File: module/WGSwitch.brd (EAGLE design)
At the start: 32.7 x 55.5 mm, 26 parts, among them Q1 MMBT3904, Q2 MMBT3904, Q3 MMBT3904, U1 7805TV, U2 ARDUINO_PRO_MINI

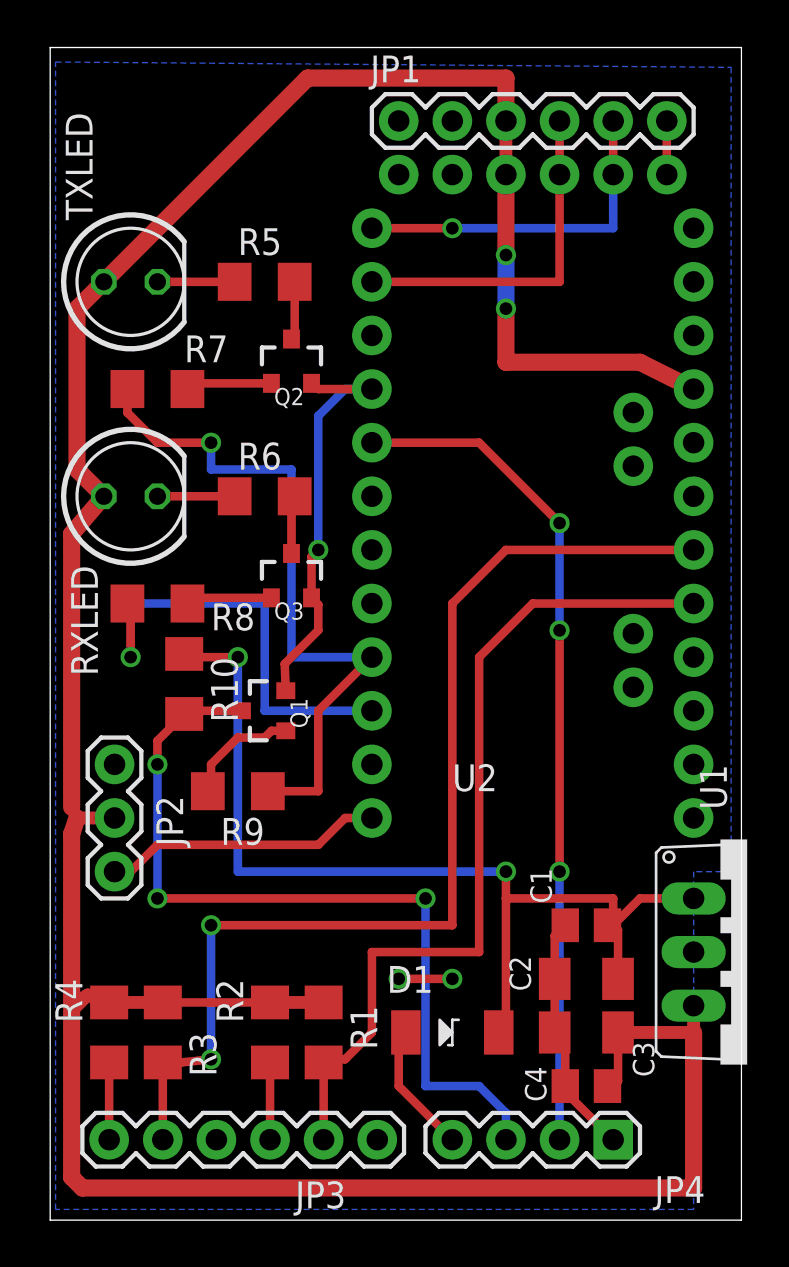
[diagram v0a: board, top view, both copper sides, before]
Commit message: cleanup and optimize TRSwitchSleep to eliminate extra delay.
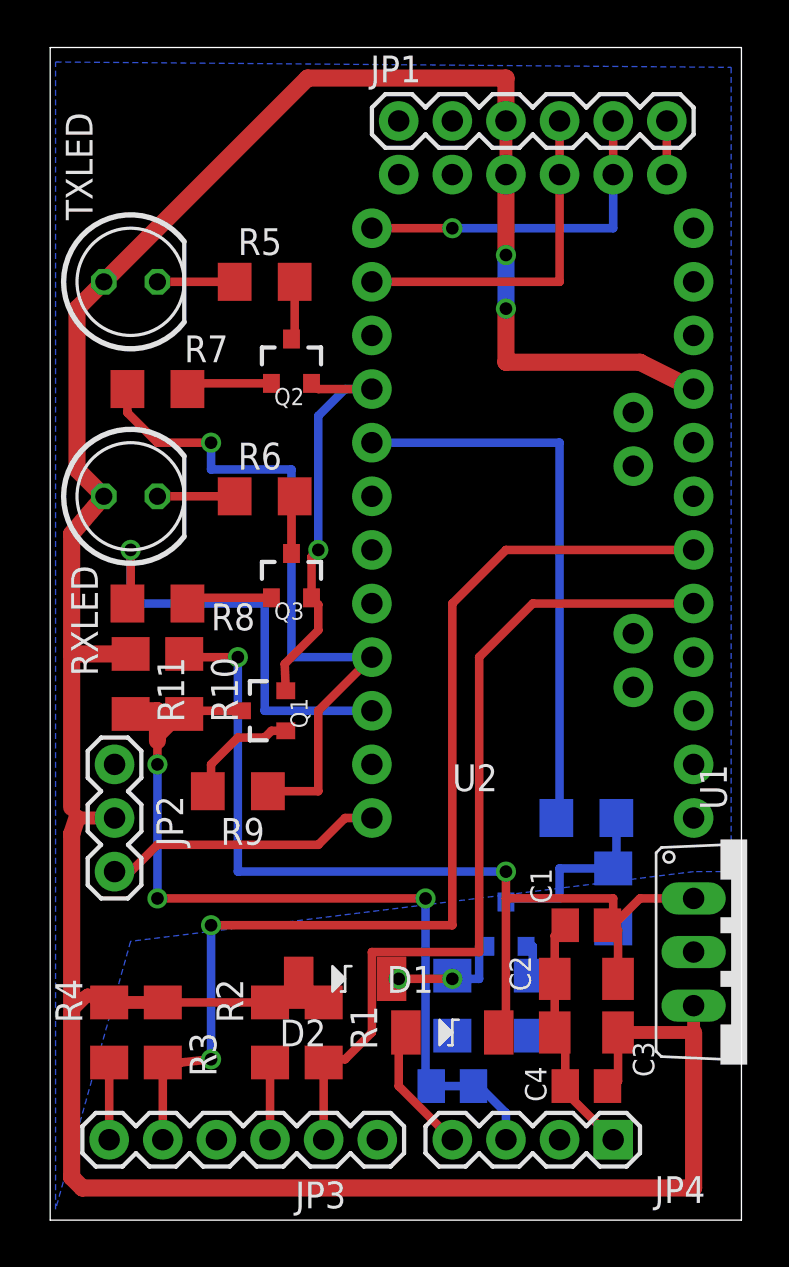
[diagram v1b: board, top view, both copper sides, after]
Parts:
- added C5: 0.1, rcl:C0805K
- added D2: PMEG3030EP, kb1vc_robot_parts:SOD128
- added Q4: PMBT3906, SparkFun-DiscreteSemi:SOT23-3
- added R11, R12, R13, R14, R15: 10K, rcl:R1206
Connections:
- removed net PTT_IN_L: JP4.2, U2.5
- new net N$12: Q4.3, R14.2, R15.2
- new net N$5: D2.P$2, Q4.2, R12.2
- new net N$9: Q4.1, R13.1
- new net PTT_H: R15.1, U2.5
- new net PTT_IN_RAW_L: C5.1, JP4.2, R12.1, R13.2
- net GND: now also C5.2, R14.1
- net TX_EN_OUT_L: now also R11.2
- net VCC: now also D2.P$1, R11.1
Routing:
- net PTT_IN_L: track 39.7 -> 0.00 mm, vias 3 -> 0
- net PTT_H: track 0.00 -> 26.8 mm
- net N$12: track 0.00 -> 9.21 mm
- net N$5: track 0.00 -> 3.28 mm
- net TX_EN_OUT_L: track 39.2 -> 42.1 mm
- net VCC: track 149.5 -> 152.3 mm
- net N$9: track 0.00 -> 1.71 mm
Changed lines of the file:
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@@
 <?xml version="1.0" encoding="utf-8"?>
 <!DOCTYPE eagle SYSTEM "eagle.dtd">
-<eagle version="7.5.0">
+<eagle version="7.3.0">
 <drawing>
 <settings>
@@
 <layer number="19" name="Unrouted" color="6" fill="1" visible="yes" active="yes"/>
 <layer number="20" name="Dimension" color="15" fill="1" visible="yes" active="yes"/>
-<layer number="21" name="tPlace" color="7" fill="1" visible="yes" active="yes"/>
-<layer number="22" name="bPlace" color="7" fill="1" visible="yes" active="yes"/>
+<layer number="21" name="tPlace" color="7" fill="1" visible="no" active="yes"/>
+<layer number="22" name="bPlace" color="7" fill="1" visible="no" active="yes"/>
 <layer number="23" name="tOrigins" color="15" fill="1" visible="yes" active="yes"/>
 <layer number="24" name="bOrigins" color="15" fill="1" visible="yes" active="yes"/>
@@
 <attribute name="VALUE" x="25.4" y="17.78" size="1.27" layer="27" ratio="10" rot="R270"/>
 </element>
+<element name="R11" library="rcl" package="R1206" value="10K" x="3.81" y="25.4" rot="R270"/>
+<element name="Q4" library="SparkFun-DiscreteSemi" package="SOT23-3" value="PMBT3906" x="21.59" y="13.97" rot="MR0">
+<attribute name="PROD_ID" value="TRANS-08052" x="21.59" y="13.97" size="1.778" layer="28" rot="MR0" display="off"/>
+</element>
+<element name="D2" library="kb1vc_robot_parts" package="SOD128" value="PMEG3030EP" x="13.97" y="11.43"/>
+<element name="R12" library="rcl" package="R1206" value="10K" x="19.05" y="10.16" rot="MR90"/>
+<element name="R13" library="rcl" package="R1206" value="10K" x="22.86" y="10.16" rot="MR270"/>
+<element name="C5" library="rcl" package="C0805K" value="0.1" x="19.05" y="6.35" rot="MR0"/>
+<element name="R14" library="rcl" package="R1206" value="10K" x="26.67" y="15.24" rot="MR90"/>
+<element name="R15" library="rcl" package="R1206" value="10K" x="25.4" y="19.05" rot="MR180"/>
 </elements>
 <signals>
@@
 <vertex x="32.258" y="16.51"/>
 <vertex x="30.48" y="16.51"/>
-<vertex x="30.48" y="0.508"/>
+<vertex x="3.81" y="13.208"/>
 <vertex x="0.254" y="0.508"/>
 </polygon>
@@
 <via x="19.05" y="11.43" extent="1-16" drill="0.6" shape="square"/>
 <wire x1="16.51" y1="11.43" x2="19.05" y2="11.43" width="0.4064" layer="1"/>
+<contactref element="C5" pad="2"/>
+<contactref element="R14" pad="1"/>
+<wire x1="26.67" y1="13.818" x2="30.48" y2="12.7" width="0" layer="19" extent="16-16"/>
+<wire x1="24.4" y1="13.97" x2="26.67" y2="13.818" width="0" layer="19" extent="1-16"/>
+<wire x1="19.05" y1="11.43" x2="23.9" y2="11.43" width="0" layer="19" extent="1-1"/>
+<wire x1="18.05" y1="6.35" x2="19.05" y2="11.43" width="0" layer="19" extent="16-16"/>
+<wire x1="15.494" y1="3.81" x2="18.05" y2="6.35" width="0" layer="19" extent="16-16"/>
+<wire x1="7.874" y1="3.81" x2="15.494" y2="3.81" width="0" layer="19" extent="1-1"/>
+<wire x1="11.16" y1="25.08" x2="16.51" y2="11.43" width="0" layer="19" extent="1-1"/>
 </signal>
 <signal name="VCC">
@@
 <wire x1="3.048" y1="19.05" x2="1.27" y2="19.05" width="0.6096" layer="1"/>
 <wire x1="1.27" y1="19.05" x2="1.016" y2="19.558" width="0.6096" layer="1"/>
-<wire x1="1.016" y1="19.558" x2="1.016" y2="32.512" width="0.8128" layer="1"/>
+<wire x1="1.016" y1="19.558" x2="1.016" y2="26.822" width="0.8128" layer="1"/>
+<wire x1="1.016" y1="26.822" x2="1.016" y2="32.512" width="0.8128" layer="1"/>
 <wire x1="1.016" y1="32.512" x2="2.54" y2="34.29" width="0.8128" layer="1"/>
 <wire x1="2.54" y1="44.45" x2="12.192" y2="54.102" width="0.8128" layer="1"/>
@@
 <wire x1="1.016" y1="9.906" x2="1.778" y2="10.668" width="0.6096" layer="1"/>
 <wire x1="5.334" y1="10.312" x2="10.414" y2="10.312" width="0.4064" layer="1"/>
+<contactref element="R11" pad="1"/>
+<wire x1="3.81" y1="26.822" x2="1.016" y2="26.822" width="0.8128" layer="1"/>
+<contactref element="D2" pad="P$1"/>
+<wire x1="12.954" y1="10.312" x2="11.77" y2="11.43" width="0" layer="19" extent="1-1"/>
 </signal>
 <signal name="N$10">
@@
 <contactref element="R8" pad="1"/>
 <contactref element="U2" pad="10"/>
-<via x="3.81" y="26.67" extent="1-16" drill="0.6" shape="square"/>
-<wire x1="3.81" y1="26.67" x2="3.81" y2="29.058" width="0.4064" layer="1"/>
+<via x="3.81" y="31.75" extent="1-16" drill="0.6" shape="square"/>
+<wire x1="3.81" y1="31.75" x2="3.81" y2="29.058" width="0.4064" layer="1"/>
 <wire x1="3.81" y1="29.058" x2="3.658" y2="29.21" width="0.4064" layer="1"/>
-<wire x1="3.81" y1="26.67" x2="3.81" y2="29.21" width="0.4064" layer="16"/>
+<wire x1="3.81" y1="31.75" x2="3.81" y2="29.21" width="0.4064" layer="16"/>
 <wire x1="3.81" y1="29.21" x2="10.16" y2="29.21" width="0.4064" layer="16"/>
 <wire x1="10.16" y1="29.21" x2="10.16" y2="24.13" width="0.4064" layer="16"/>
@@
 <wire x1="7.62" y1="36.83" x2="5.08" y2="36.83" width="0.4064" layer="1"/>
 <wire x1="5.08" y1="36.83" x2="3.658" y2="38.252" width="0.4064" layer="1"/>
-</signal>
-<signal name="PTT_IN_L">
-<contactref element="JP4" pad="2"/>
-<contactref element="U2" pad="5"/>
-<wire x1="15.24" y1="36.83" x2="20.32" y2="36.83" width="0.4064" layer="1"/>
-<wire x1="20.32" y1="36.83" x2="24.13" y2="33.02" width="0.4064" layer="1"/>
-<via x="24.13" y="33.02" extent="1-16" drill="0.6" shape="square"/>
-<wire x1="24.13" y1="33.02" x2="24.13" y2="27.94" width="0.4064" layer="16"/>
-<via x="24.13" y="27.94" extent="1-16" drill="0.6" shape="square"/>
-<wire x1="24.13" y1="27.94" x2="24.13" y2="16.51" width="0.4064" layer="1"/>
-<via x="24.13" y="16.51" extent="1-16" drill="0.6" shape="square"/>
-<wire x1="24.13" y1="16.51" x2="24.13" y2="3.81" width="0.4064" layer="16"/>
 </signal>
 <signal name="TX_EN_OUT_L">
@@
 <wire x1="20.32" y1="6.35" x2="21.59" y2="5.08" width="0.4064" layer="16"/>
 <wire x1="21.59" y1="5.08" x2="21.59" y2="3.81" width="0.4064" layer="16"/>
+<contactref element="R11" pad="2"/>
+<wire x1="5.08" y1="22.708" x2="5.08" y2="24.13" width="0.8128" layer="1"/>
+<wire x1="5.08" y1="24.13" x2="3.81" y2="24.13" width="0.8128" layer="1"/>
+<wire x1="3.81" y1="24.13" x2="3.81" y2="23.978" width="0.8128" layer="1"/>
 </signal>
 <signal name="N$2">
@@
 <wire x1="6.772" y1="39.64" x2="6.502" y2="39.37" width="0.4064" layer="1"/>
 </signal>
+<signal name="PTT_IN_RAW_L">
+<contactref element="JP4" pad="2"/>
+<contactref element="R12" pad="1"/>
+<contactref element="C5" pad="1"/>
+<contactref element="R13" pad="2"/>
+<wire x1="20.05" y1="6.35" x2="22.86" y2="8.738" width="0" layer="19" extent="16-16"/>
+<wire x1="19.05" y1="8.738" x2="20.05" y2="6.35" width="0" layer="19" extent="16-16"/>
+<wire x1="24.13" y1="3.81" x2="20.05" y2="6.35" width="0" layer="19" extent="16-16"/>
+</signal>
+<signal name="N$5">
+<contactref element="D2" pad="P$2"/>
+<contactref element="Q4" pad="2"/>
+<contactref element="R12" pad="2"/>
+<wire x1="16.17" y1="11.43" x2="19.05" y2="11.582" width="0" layer="19" extent="1-16"/>
+<wire x1="20.64" y1="12.97" x2="20.32" y2="12.97" width="0.4064" layer="16"/>
+<wire x1="20.32" y1="12.97" x2="20.32" y2="11.43" width="0.4064" layer="16"/>
+<wire x1="20.32" y1="11.43" x2="19.05" y2="11.43" width="0.4064" layer="16"/>
+<wire x1="19.05" y1="11.43" x2="19.05" y2="11.582" width="0.4064" layer="16"/>
+</signal>
+<signal name="N$9">
+<contactref element="Q4" pad="1"/>
+<contactref element="R13" pad="1"/>
+<wire x1="22.54" y1="12.97" x2="22.86" y2="12.97" width="0.4064" layer="16"/>
+<wire x1="22.86" y1="12.97" x2="22.86" y2="11.582" width="0.4064" layer="16"/>
+</signal>
+<signal name="N$12">
+<contactref element="Q4" pad="3"/>
+<contactref element="R14" pad="2"/>
+<contactref element="R15" pad="2"/>
+<wire x1="26.67" y1="16.662" x2="26.822" y2="16.662" width="0.4064" layer="16"/>
+<wire x1="26.822" y1="16.662" x2="26.822" y2="19.05" width="0.4064" layer="16"/>
+<wire x1="26.67" y1="16.662" x2="24.13" y2="16.662" width="0.4064" layer="16"/>
+<wire x1="24.13" y1="16.662" x2="24.13" y2="15.24" width="0.4064" layer="16"/>
+<wire x1="24.13" y1="15.24" x2="21.59" y2="15.24" width="0.4064" layer="16"/>
+<wire x1="21.59" y1="15.24" x2="21.59" y2="15.07" width="0.4064" layer="16"/>
+</signal>
+<signal name="PTT_H">
+<contactref element="R15" pad="1"/>
+<contactref element="U2" pad="5"/>
+<wire x1="23.978" y1="19.05" x2="24.13" y2="19.05" width="0.4064" layer="16"/>
+<wire x1="24.13" y1="19.05" x2="24.13" y2="36.83" width="0.4064" layer="16"/>
+<wire x1="24.13" y1="36.83" x2="15.24" y2="36.83" width="0.4064" layer="16"/>
+</signal>
 </signals>

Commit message: Just about right.
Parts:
- removed C5: 0.1, rcl:C0805K
- removed D2: PMEG3030EP, kb1vc_robot_parts:SOD128
- removed Q4: PMBT3906, SparkFun-DiscreteSemi:SOT23-3
- removed R11, R12, R13, R14, R15: 10K, rcl:R1206
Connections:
- removed net N$12: Q4.3, R14.2, R15.2
- removed net N$5: D2.P$2, Q4.2, R12.2
- removed net N$9: Q4.1, R13.1
- removed net PTT_H: R15.1, U2.5
- removed net PTT_IN_RAW_L: C5.1, JP4.2, R12.1, R13.2
- new net PTT_IN_L: JP4.2, U2.5
- net GND: no longer C5.2, R14.1
- net TX_EN_OUT_L: no longer R11.2
- net VCC: no longer D2.P$1, R11.1
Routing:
- net PTT_IN_L: track 0.00 -> 39.7 mm, vias 0 -> 3
- net PTT_H: track 26.8 -> 0.00 mm
- net N$12: track 9.21 -> 0.00 mm
- net N$5: track 3.28 -> 0.00 mm
- net TX_EN_OUT_L: track 42.1 -> 39.2 mm
- net VCC: track 152.3 -> 149.5 mm
- net N$9: track 1.71 -> 0.00 mm
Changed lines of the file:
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@@
 <?xml version="1.0" encoding="utf-8"?>
 <!DOCTYPE eagle SYSTEM "eagle.dtd">
-<eagle version="7.3.0">
+<eagle version="7.5.0">
 <drawing>
 <settings>
@@
 <layer number="19" name="Unrouted" color="6" fill="1" visible="yes" active="yes"/>
 <layer number="20" name="Dimension" color="15" fill="1" visible="yes" active="yes"/>
-<layer number="21" name="tPlace" color="7" fill="1" visible="no" active="yes"/>
-<layer number="22" name="bPlace" color="7" fill="1" visible="no" active="yes"/>
+<layer number="21" name="tPlace" color="7" fill="1" visible="yes" active="yes"/>
+<layer number="22" name="bPlace" color="7" fill="1" visible="yes" active="yes"/>
 <layer number="23" name="tOrigins" color="15" fill="1" visible="yes" active="yes"/>
 <layer number="24" name="bOrigins" color="15" fill="1" visible="yes" active="yes"/>
@@
 <attribute name="VALUE" x="25.4" y="17.78" size="1.27" layer="27" ratio="10" rot="R270"/>
 </element>
-<element name="R11" library="rcl" package="R1206" value="10K" x="3.81" y="25.4" rot="R270"/>
-<element name="Q4" library="SparkFun-DiscreteSemi" package="SOT23-3" value="PMBT3906" x="21.59" y="13.97" rot="MR0">
-<attribute name="PROD_ID" value="TRANS-08052" x="21.59" y="13.97" size="1.778" layer="28" rot="MR0" display="off"/>
-</element>
-<element name="D2" library="kb1vc_robot_parts" package="SOD128" value="PMEG3030EP" x="13.97" y="11.43"/>
-<element name="R12" library="rcl" package="R1206" value="10K" x="19.05" y="10.16" rot="MR90"/>
-<element name="R13" library="rcl" package="R1206" value="10K" x="22.86" y="10.16" rot="MR270"/>
-<element name="C5" library="rcl" package="C0805K" value="0.1" x="19.05" y="6.35" rot="MR0"/>
-<element name="R14" library="rcl" package="R1206" value="10K" x="26.67" y="15.24" rot="MR90"/>
-<element name="R15" library="rcl" package="R1206" value="10K" x="25.4" y="19.05" rot="MR180"/>
 </elements>
 <signals>
@@
 <vertex x="32.258" y="16.51"/>
 <vertex x="30.48" y="16.51"/>
-<vertex x="3.81" y="13.208"/>
+<vertex x="30.48" y="0.508"/>
 <vertex x="0.254" y="0.508"/>
 </polygon>
@@
 <via x="19.05" y="11.43" extent="1-16" drill="0.6" shape="square"/>
 <wire x1="16.51" y1="11.43" x2="19.05" y2="11.43" width="0.4064" layer="1"/>
-<contactref element="C5" pad="2"/>
-<contactref element="R14" pad="1"/>
-<wire x1="26.67" y1="13.818" x2="30.48" y2="12.7" width="0" layer="19" extent="16-16"/>
-<wire x1="24.4" y1="13.97" x2="26.67" y2="13.818" width="0" layer="19" extent="1-16"/>
-<wire x1="19.05" y1="11.43" x2="23.9" y2="11.43" width="0" layer="19" extent="1-1"/>
-<wire x1="18.05" y1="6.35" x2="19.05" y2="11.43" width="0" layer="19" extent="16-16"/>
-<wire x1="15.494" y1="3.81" x2="18.05" y2="6.35" width="0" layer="19" extent="16-16"/>
-<wire x1="7.874" y1="3.81" x2="15.494" y2="3.81" width="0" layer="19" extent="1-1"/>
-<wire x1="11.16" y1="25.08" x2="16.51" y2="11.43" width="0" layer="19" extent="1-1"/>
 </signal>
 <signal name="VCC">
@@
 <wire x1="3.048" y1="19.05" x2="1.27" y2="19.05" width="0.6096" layer="1"/>
 <wire x1="1.27" y1="19.05" x2="1.016" y2="19.558" width="0.6096" layer="1"/>
-<wire x1="1.016" y1="19.558" x2="1.016" y2="26.822" width="0.8128" layer="1"/>
-<wire x1="1.016" y1="26.822" x2="1.016" y2="32.512" width="0.8128" layer="1"/>
+<wire x1="1.016" y1="19.558" x2="1.016" y2="32.512" width="0.8128" layer="1"/>
 <wire x1="1.016" y1="32.512" x2="2.54" y2="34.29" width="0.8128" layer="1"/>
 <wire x1="2.54" y1="44.45" x2="12.192" y2="54.102" width="0.8128" layer="1"/>
@@
 <wire x1="1.016" y1="9.906" x2="1.778" y2="10.668" width="0.6096" layer="1"/>
 <wire x1="5.334" y1="10.312" x2="10.414" y2="10.312" width="0.4064" layer="1"/>
-<contactref element="R11" pad="1"/>
-<wire x1="3.81" y1="26.822" x2="1.016" y2="26.822" width="0.8128" layer="1"/>
-<contactref element="D2" pad="P$1"/>
-<wire x1="12.954" y1="10.312" x2="11.77" y2="11.43" width="0" layer="19" extent="1-1"/>
 </signal>
 <signal name="N$10">
@@
 <contactref element="R8" pad="1"/>
 <contactref element="U2" pad="10"/>
-<via x="3.81" y="31.75" extent="1-16" drill="0.6" shape="square"/>
-<wire x1="3.81" y1="31.75" x2="3.81" y2="29.058" width="0.4064" layer="1"/>
+<via x="3.81" y="26.67" extent="1-16" drill="0.6" shape="square"/>
+<wire x1="3.81" y1="26.67" x2="3.81" y2="29.058" width="0.4064" layer="1"/>
 <wire x1="3.81" y1="29.058" x2="3.658" y2="29.21" width="0.4064" layer="1"/>
-<wire x1="3.81" y1="31.75" x2="3.81" y2="29.21" width="0.4064" layer="16"/>
+<wire x1="3.81" y1="26.67" x2="3.81" y2="29.21" width="0.4064" layer="16"/>
 <wire x1="3.81" y1="29.21" x2="10.16" y2="29.21" width="0.4064" layer="16"/>
 <wire x1="10.16" y1="29.21" x2="10.16" y2="24.13" width="0.4064" layer="16"/>
@@
 <wire x1="7.62" y1="36.83" x2="5.08" y2="36.83" width="0.4064" layer="1"/>
 <wire x1="5.08" y1="36.83" x2="3.658" y2="38.252" width="0.4064" layer="1"/>
+</signal>
+<signal name="PTT_IN_L">
+<contactref element="JP4" pad="2"/>
+<contactref element="U2" pad="5"/>
+<wire x1="15.24" y1="36.83" x2="20.32" y2="36.83" width="0.4064" layer="1"/>
+<wire x1="20.32" y1="36.83" x2="24.13" y2="33.02" width="0.4064" layer="1"/>
+<via x="24.13" y="33.02" extent="1-16" drill="0.6" shape="square"/>
+<wire x1="24.13" y1="33.02" x2="24.13" y2="27.94" width="0.4064" layer="16"/>
+<via x="24.13" y="27.94" extent="1-16" drill="0.6" shape="square"/>
+<wire x1="24.13" y1="27.94" x2="24.13" y2="16.51" width="0.4064" layer="1"/>
+<via x="24.13" y="16.51" extent="1-16" drill="0.6" shape="square"/>
+<wire x1="24.13" y1="16.51" x2="24.13" y2="3.81" width="0.4064" layer="16"/>
 </signal>
 <signal name="TX_EN_OUT_L">
@@
 <wire x1="20.32" y1="6.35" x2="21.59" y2="5.08" width="0.4064" layer="16"/>
 <wire x1="21.59" y1="5.08" x2="21.59" y2="3.81" width="0.4064" layer="16"/>
-<contactref element="R11" pad="2"/>
-<wire x1="5.08" y1="22.708" x2="5.08" y2="24.13" width="0.8128" layer="1"/>
-<wire x1="5.08" y1="24.13" x2="3.81" y2="24.13" width="0.8128" layer="1"/>
-<wire x1="3.81" y1="24.13" x2="3.81" y2="23.978" width="0.8128" layer="1"/>
 </signal>
 <signal name="N$2">
@@
 <wire x1="6.772" y1="39.64" x2="6.502" y2="39.37" width="0.4064" layer="1"/>
 </signal>
-<signal name="PTT_IN_RAW_L">
-<contactref element="JP4" pad="2"/>
-<contactref element="R12" pad="1"/>
-<contactref element="C5" pad="1"/>
-<contactref element="R13" pad="2"/>
-<wire x1="20.05" y1="6.35" x2="22.86" y2="8.738" width="0" layer="19" extent="16-16"/>
-<wire x1="19.05" y1="8.738" x2="20.05" y2="6.35" width="0" layer="19" extent="16-16"/>
-<wire x1="24.13" y1="3.81" x2="20.05" y2="6.35" width="0" layer="19" extent="16-16"/>
-</signal>
-<signal name="N$5">
-<contactref element="D2" pad="P$2"/>
-<contactref element="Q4" pad="2"/>
-<contactref element="R12" pad="2"/>
-<wire x1="16.17" y1="11.43" x2="19.05" y2="11.582" width="0" layer="19" extent="1-16"/>
-<wire x1="20.64" y1="12.97" x2="20.32" y2="12.97" width="0.4064" layer="16"/>
-<wire x1="20.32" y1="12.97" x2="20.32" y2="11.43" width="0.4064" layer="16"/>
-<wire x1="20.32" y1="11.43" x2="19.05" y2="11.43" width="0.4064" layer="16"/>
-<wire x1="19.05" y1="11.43" x2="19.05" y2="11.582" width="0.4064" layer="16"/>
-</signal>
-<signal name="N$9">
-<contactref element="Q4" pad="1"/>
-<contactref element="R13" pad="1"/>
-<wire x1="22.54" y1="12.97" x2="22.86" y2="12.97" width="0.4064" layer="16"/>
-<wire x1="22.86" y1="12.97" x2="22.86" y2="11.582" width="0.4064" layer="16"/>
-</signal>
-<signal name="N$12">
-<contactref element="Q4" pad="3"/>
-<contactref element="R14" pad="2"/>
-<contactref element="R15" pad="2"/>
-<wire x1="26.67" y1="16.662" x2="26.822" y2="16.662" width="0.4064" layer="16"/>
-<wire x1="26.822" y1="16.662" x2="26.822" y2="19.05" width="0.4064" layer="16"/>
-<wire x1="26.67" y1="16.662" x2="24.13" y2="16.662" width="0.4064" layer="16"/>
-<wire x1="24.13" y1="16.662" x2="24.13" y2="15.24" width="0.4064" layer="16"/>
-<wire x1="24.13" y1="15.24" x2="21.59" y2="15.24" width="0.4064" layer="16"/>
-<wire x1="21.59" y1="15.24" x2="21.59" y2="15.07" width="0.4064" layer="16"/>
-</signal>
-<signal name="PTT_H">
-<contactref element="R15" pad="1"/>
-<contactref element="U2" pad="5"/>
-<wire x1="23.978" y1="19.05" x2="24.13" y2="19.05" width="0.4064" layer="16"/>
-<wire x1="24.13" y1="19.05" x2="24.13" y2="36.83" width="0.4064" layer="16"/>
-<wire x1="24.13" y1="36.83" x2="15.24" y2="36.83" width="0.4064" layer="16"/>
-</signal>
 </signals>
